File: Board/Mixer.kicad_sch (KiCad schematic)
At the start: 30 parts, among them IC26 LM3900N, X4 1503_09

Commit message: Ultipet 1.0A final
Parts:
- removed C142: 100n, cbm_ultipet_v1:C025-024X044, symbol cbm_ultipet_v1-eagle-import:C-EU025-024X044

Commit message: ultipet 1.1a board
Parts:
- added C129, C136: 1u, cbm_ultipet_v1:E2-5, symbol cbm_ultipet_v1-eagle-import:CPOL-EUE2-5
- added C138, C142, C143, C144: 100n, cbm_ultipet_v1:C025-024X044, symbol cbm_ultipet_v1-eagle-import:C-EU025-024X044
- added JP18, JP9: JP1E, cbm_ultipet_v1:JP1, symbol cbm_ultipet_v1-eagle-import:JP1E
- added R21, R3: 470, cbm_ultipet_v1:0204_7, symbol cbm_ultipet_v1-eagle-import:R-EU_0204/7
- added RV1: R_Potentiometer_Dual, cbm_ultipet_v1:RK12L12_horizontal, symbol Device:R_Potentiometer_Dual
- added U6, U7: LM386, Package_DIP:DIP-8_W7.62mm_Socket_LongPads, symbol Amplifier_Audio:LM386
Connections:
- net BEEPER: now also R3.1; no longer C82.+, C83.+
- net GND: now also C138.2, C142.2, C143.2, C144.2, JP18.2, JP9.2, R21.2, RV1.3, RV1.6, U6.2 (-), U6.4 (GND), U7.2 (-), U7.4 (GND)
- net VCC: now also C143.1, C144.1, U6.6 (V+), U7.6 (V+)
- net at X4.4: now also RV1.1
- net at X4.5: now also RV1.4
- new net: RV1.5, U7.3 (+)
- new net: C136.+, C142.1, U7.5
- new net: C82.+, C83.+, R21.1, R3.2
- new net: C129.+, C138.1, U6.5
- new net: C129.-, JP9.1
- new net: RV1.2, U6.3 (+)
- new net: C136.-, JP18.1
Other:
- note added: "1.0B: add voltage divider to reduce beeper volume on mixer output"
- note added: "CBM-ULTIPET-1.0B-20240502"
- note added: "CBM-ULTIPET-V1.1A"
- note added: "Left Speaker"
- note added: "Right Speaker"
- note removed: "CBM-ULTIPET-1.0A-20240104"
- note removed: "CBM-ULTIPET-V1.0A"
- moved on the sheet: C141, C82, C83

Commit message: diverse fixes
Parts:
- added R27: 4k7, cbm_ultipet_v1:0204_7, symbol cbm_ultipet_v1-eagle-import:R-EU_0204/7
- added R32: 470, cbm_ultipet_v1:0204_7, symbol cbm_ultipet_v1-eagle-import:R-EU_0204/7
- R3: value 470 -> 4k7
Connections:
- net BEEPER: now also R27.1
- net GND: now also RV1.1, RV1.4, R32.2; no longer RV1.3, RV1.6
- net at C82.+, R21.1, R3.2: no longer C83.+
- net at X4.4: now also RV1.3; no longer RV1.1
- net at X4.5: now also RV1.6; no longer RV1.4
- new net: C83.+, R27.2, R32.1
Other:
- note added: "1.0B: add voltage divider to reduce beeper volume on mixer output 1.2A: - duplicate beeper voltage divider to reduce L/R crosstalk - adjust beeper voltage divider resistor values"
- note added: "CBM-ULTIPET-1.2A-20241010"
- note added: "CBM-ULTIPET-V1.2A"
- note removed: "1.0B: add voltage divider to reduce beeper volume on mixer output"
- note removed: "CBM-ULTIPET-1.0B-20240502"
- note removed: "CBM-ULTIPET-V1.1A"

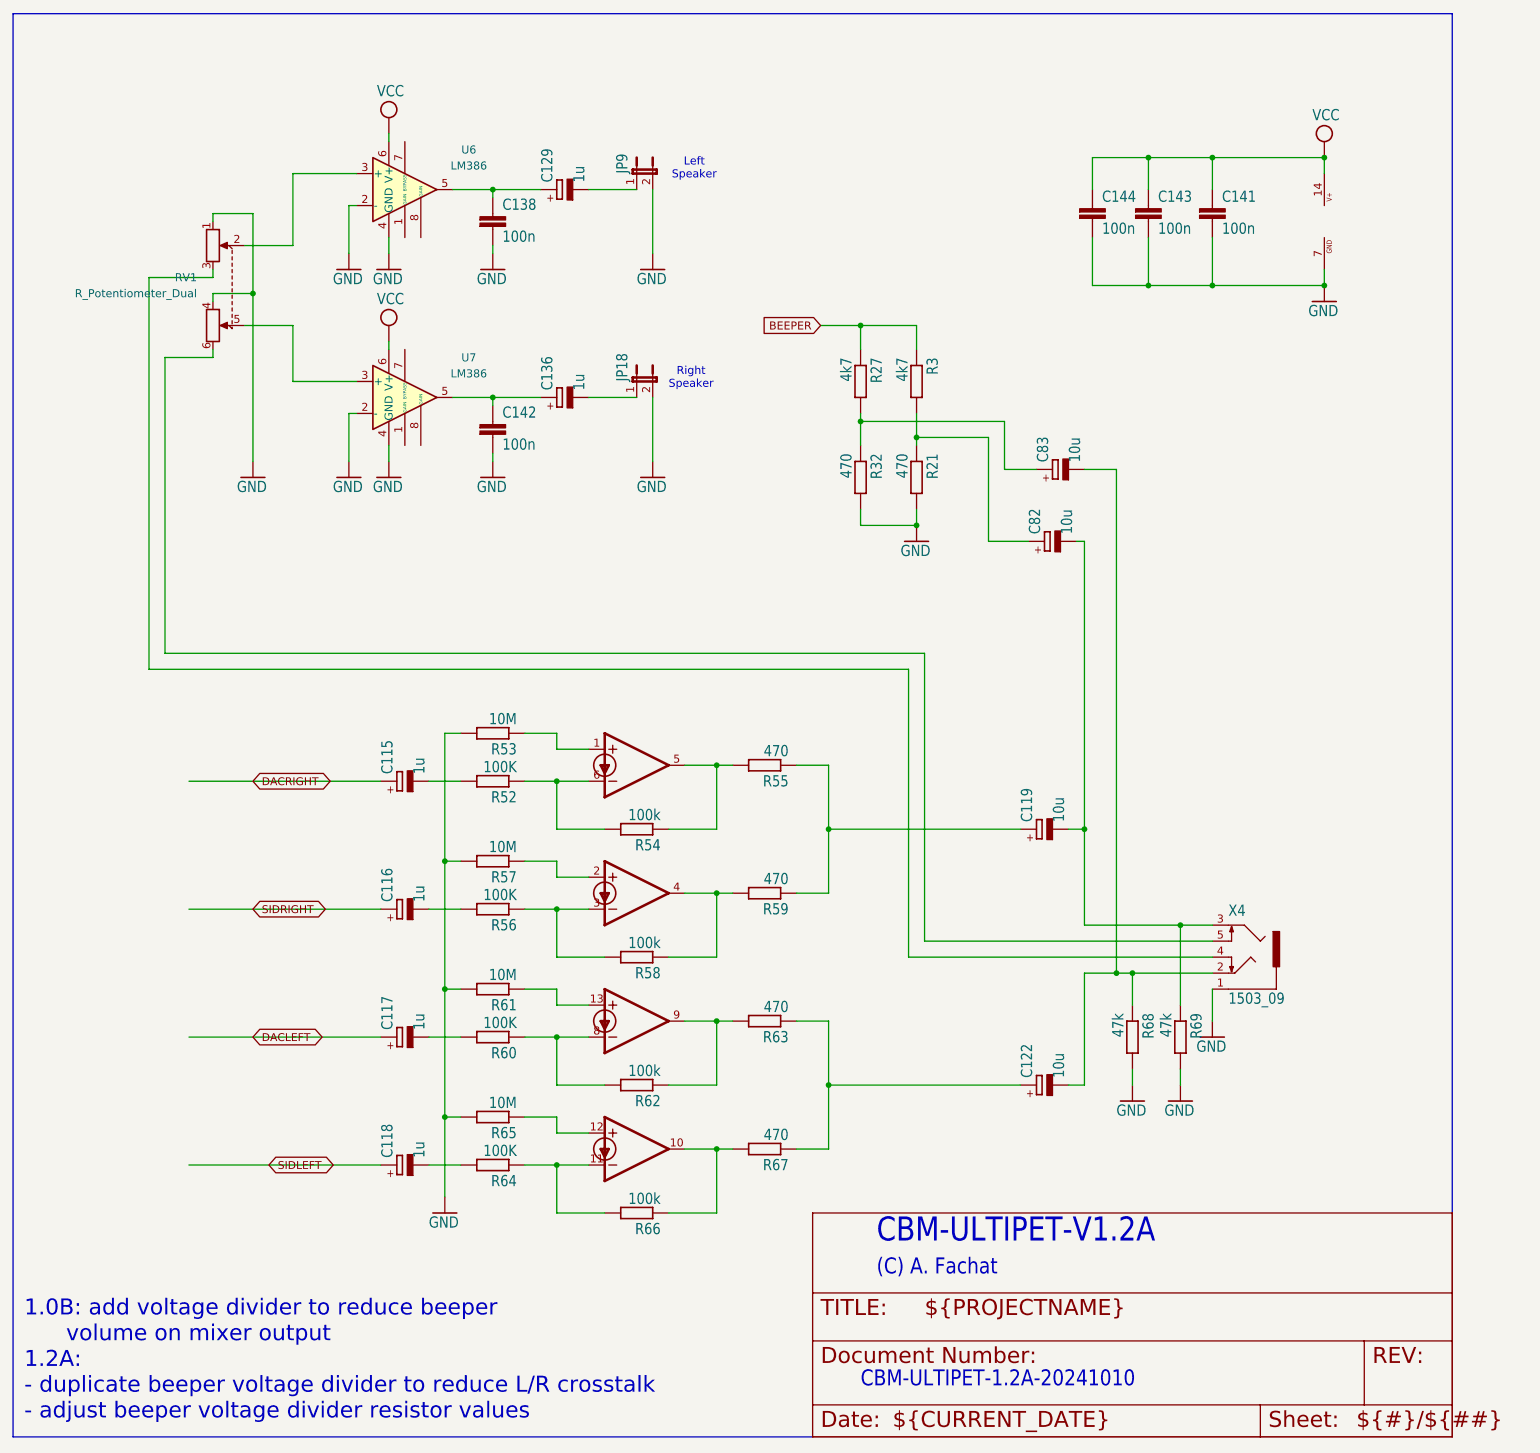
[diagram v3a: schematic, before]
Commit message: improve mixer, reduce noise
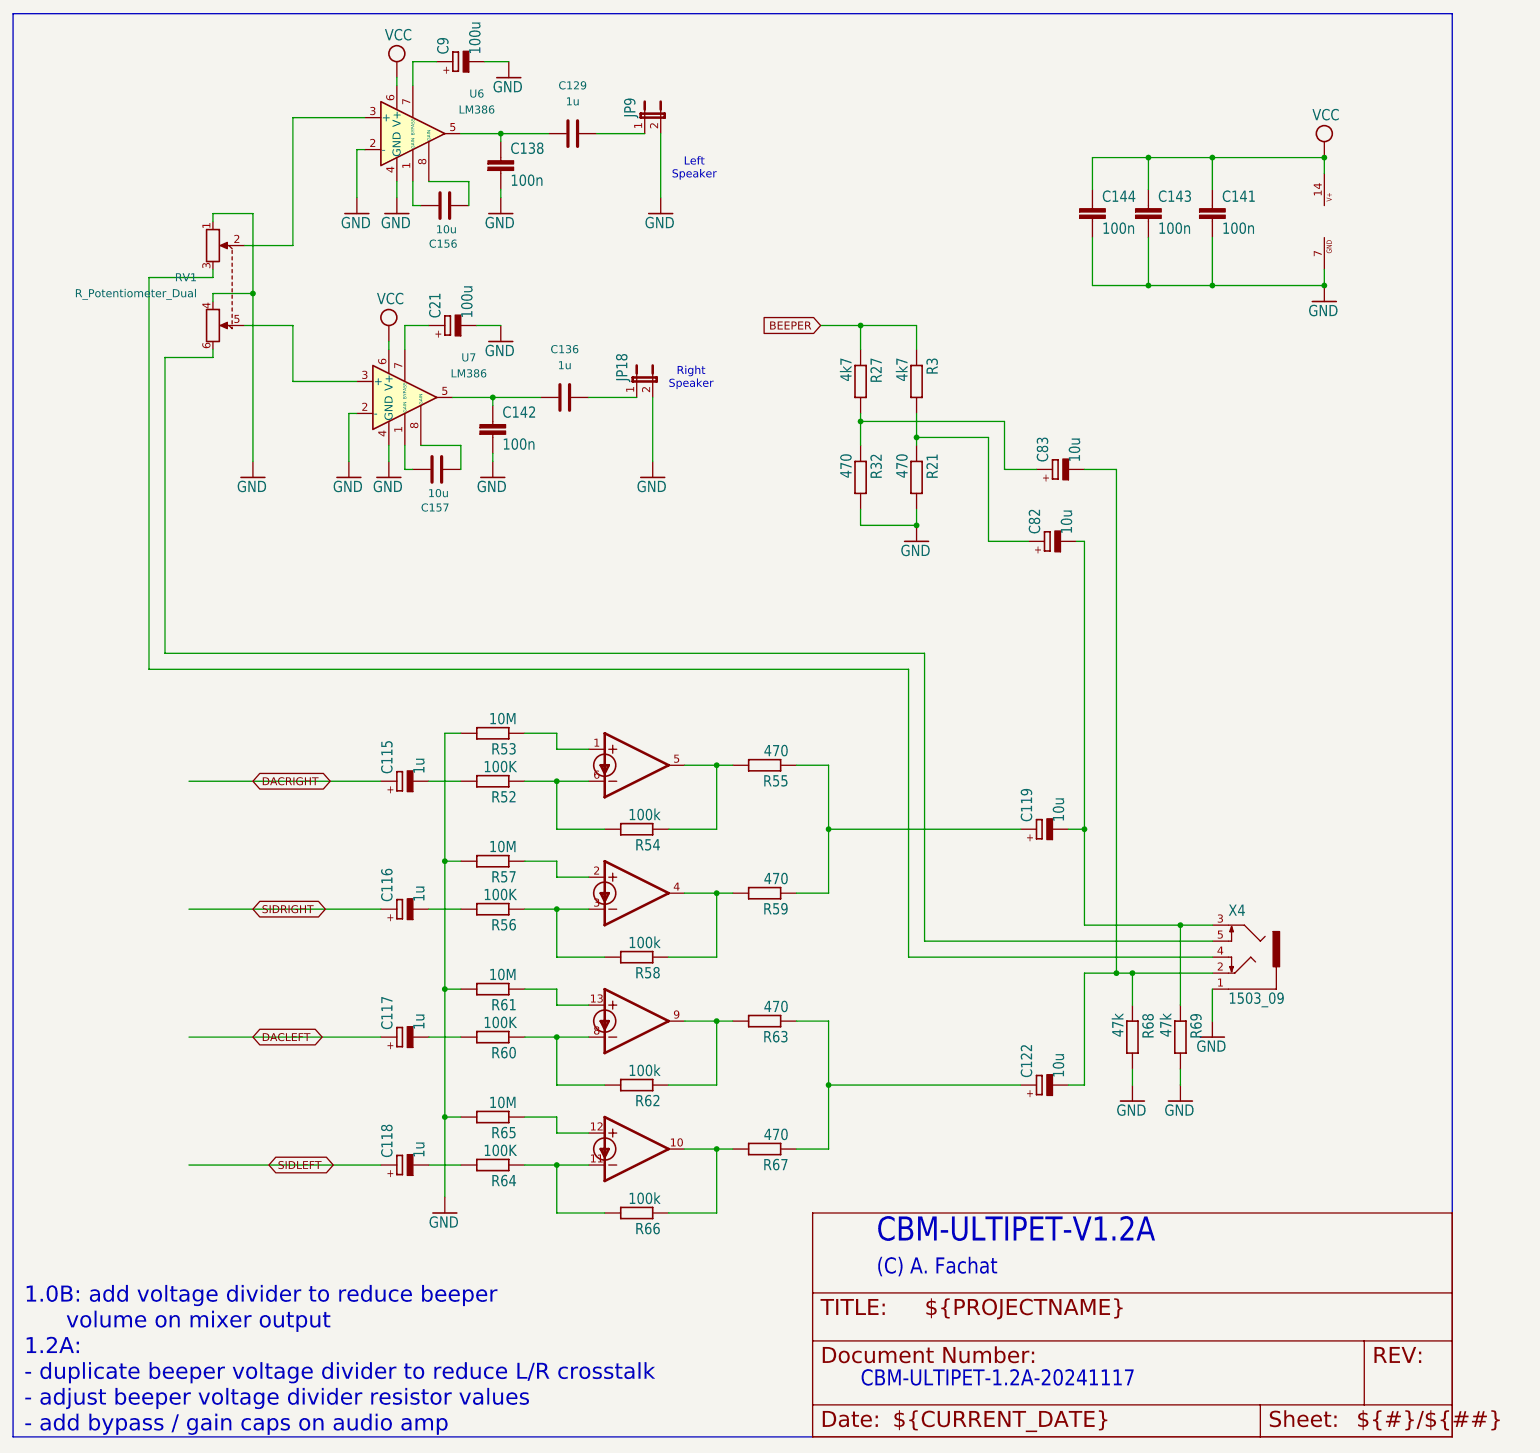
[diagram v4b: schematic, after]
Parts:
- removed C129, C136: 1u, cbm_ultipet_v1:E2-5, symbol cbm_ultipet_v1-eagle-import:CPOL-EUE2-5
- added C129, C136: 1u, Capacitor_THT:C_Disc_D5.0mm_W2.5mm_P5.00mm, symbol Device:C
- added C156, C157: 10u, Capacitor_THT:C_Disc_D5.0mm_W2.5mm_P5.00mm, symbol Device:C
- added C21, C9: 100u, cbm_ultipet_v1:E2-5, symbol cbm_ultipet_v1-eagle-import:CPOL-EUE2-5
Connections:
- net GND: now also C21.-, C9.-
- net at U7.1 (GAIN): now also C157.1
- net at C142.1, U7.5: now also C136.1
- net at U7.7 (BYPASS): now also C21.+
- net at U7.8 (GAIN): now also C157.2
- net at C138.1, U6.5: now also C129.1
- net at JP9.1: now also C129.2
- net at U6.1 (GAIN): now also C156.1
- net at U6.7 (BYPASS): now also C9.+
- net at U6.8 (GAIN): now also C156.2
- net at JP18.1: now also C136.2
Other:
- note added: "1.0B: add voltage divider to reduce beeper volume on mixer output 1.2A: - duplicate beeper voltage divider to reduce L/R crosstalk - adjust beeper voltage divider resistor values - add bypass / gain caps on audio amp"
- note added: "CBM-ULTIPET-1.2A-20241117"
- note removed: "1.0B: add voltage divider to reduce beeper volume on mixer output 1.2A: - duplicate beeper voltage divider to reduce L/R crosstalk - adjust beeper voltage divider resistor values"
- note removed: "CBM-ULTIPET-1.2A-20241010"
- moved on the sheet: C138, JP9, U6

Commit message: first work on r1.3
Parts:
- removed C129, C136: 1u, Capacitor_THT:C_Disc_D5.0mm_W2.5mm_P5.00mm, symbol Device:C
- removed C156, C157: 10u, Capacitor_THT:C_Disc_D5.0mm_W2.5mm_P5.00mm, symbol Device:C
- removed JP18, JP9: JP1E, cbm_ultipet_v1:JP1, symbol cbm_ultipet_v1-eagle-import:JP1E
- removed R68, R69: 47k, cbm_ultipet_v1:0204_7, symbol cbm_ultipet_v1-eagle-import:R-EU_0204/7
- added C129, C136: 100u, cbm_ultipet_v1:E2-5, symbol cbm_ultipet_v1-eagle-import:CPOL-EUE2-5
- added J6: Conn_01x04_Pin, Connector_PinHeader_2.54mm:PinHeader_1x04_P2.54mm_Vertical, symbol Connector:Conn_01x04_Pin
- added R34, R35: 10k, Resistor_THT:R_Axial_DIN0204_L3.6mm_D1.6mm_P2.54mm_Vertical, symbol cbm_ultipet_v1-eagle-import:R-EU_0204/7
- R53, R57, R61, R65: value 10M -> 220k
- RV1: value R_Potentiometer_Dual -> dual 10k linear
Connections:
- net GND: now also RV1.3, RV1.6, J6.2 (Pin_2), J6.3 (Pin_3); no longer R53.2, R57.2, R61.2, R65.2, RV1.1, RV1.4
- net VCC: now also R53.2, R57.2, R61.2, R65.2
- net at RV1.5, U7.3 (+): now also RV1.4, R35.2
- net at C142.1, U7.5: now also C136.+
- net at RV1.2, U6.3 (+): now also RV1.1, R34.2
- net at X4.4: now also R34.1; no longer RV1.3
- net at X4.5: now also R35.1; no longer RV1.6
- net at C138.1, U6.5: now also C129.+
- new net: C129.-, J6.4 (Pin_4)
- new net: C136.-, J6.1 (Pin_1)

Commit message: work on r1.3
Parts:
- IC26: footprint cbm_ultipet_v1:DIL14 -> Package_DIP:DIP-14_W7.62mm_Socket_LongPads
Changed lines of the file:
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@@
 			)
 		)
-		(property "Footprint" "cbm_ultipet_v1:DIL14"
+		(property "Footprint" "Package_DIP:DIP-14_W7.62mm_Socket_LongPads"
 			(at 238.76 50.8 0)
 			(effects
@@
 			)
 		)
-		(property "Footprint" "cbm_ultipet_v1:DIL14"
+		(property "Footprint" "Package_DIP:DIP-14_W7.62mm_Socket_LongPads"
 			(at 129.54 198.12 0)
 			(effects
@@
 			)
 		)
-		(property "Footprint" "cbm_ultipet_v1:DIL14"
+		(property "Footprint" "Package_DIP:DIP-14_W7.62mm_Socket_LongPads"
 			(at 129.54 137.16 0)
 			(effects
@@
 			)
 		)
-		(property "Footprint" "cbm_ultipet_v1:DIL14"
+		(property "Footprint" "Package_DIP:DIP-14_W7.62mm_Socket_LongPads"
 			(at 129.54 157.48 0)
 			(effects
@@
 			)
 		)
-		(property "Footprint" "cbm_ultipet_v1:DIL14"
+		(property "Footprint" "Package_DIP:DIP-14_W7.62mm_Socket_LongPads"
 			(at 129.54 177.8 0)
 			(effects

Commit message: preview for r1.3
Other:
- note added: "CBM-ULTIPET-V1.3A"
- note removed: "CBM-ULTIPET-V1.2A"
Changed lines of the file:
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@@
 		)
 	)
-	(text "CBM-ULTIPET-V1.2A"
+	(text "CBM-ULTIPET-V1.3A"
 		(exclude_from_sim no)
 		(at 167.64 213.36 0)
